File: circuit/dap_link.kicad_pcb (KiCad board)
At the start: 2 copper layers, 44.6 x 23.5 mm, 35 parts, among them J1 USB_A_CONN, J2 SWD_CONN_5P, J3 UART1_CONN_3P, J4 PAEX_CONN_8P, U1 STM32F103CBTx, U2 AMS1117-3.3, Y1 8MHz

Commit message: 新版kicad
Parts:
- removed J4: PAEX_CONN_8P, Connector_PinHeader_2.54mm:PinHeader_1x08_P2.54mm_Horizontal
- removed R11, R13, R14, R15, R16, R17, R18: 1K, Resistor_SMD:R_0603_1608Metric_Pad1.05x0.95mm_HandSolder
- added J5: Conn_02x10_Odd_Even, Connector_PinSocket_2.54mm:PinSocket_2x10_P2.54mm_Horizontal, B.Cu at (150.5, 114.7)
- added U3: TXS0108EPW, Package_SO:TSSOP-20_4.4x6.5mm_P0.65mm, F.Cu at (141.3, 104.1)
- C1, C2, C3, C4, C7, C8: footprint Capacitor_SMD:C_0603_1608Metric_Pad1.05x0.95mm_HandSolder -> Capacitor_SMD:C_0805_2012Metric_Pad1.18x1.45mm_HandSolder
- R1, R10, R12, R2, R3, R4, R5, R6, R7, R8, R9: footprint Resistor_SMD:R_0603_1608Metric_Pad1.05x0.95mm_HandSolder -> Resistor_SMD:R_0805_2012Metric_Pad1.20x1.40mm_HandSolder
- Y1: footprint Crystal:Crystal_SMD_HC49-SD -> Crystal:Crystal_SMD_5032-2Pin_5.0x3.2mm_HandSoldering
- moved C7 2.16 mm to (126.3, 125.9)
- moved Y1 1.97 mm to (123.0, 127.8)
- moved C4 1.92 mm to (126.2, 130.4)
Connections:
- U1 pad 17: /LEDR_GPIO -> /PA7
- U1 pad 18: Net-(U1-Pad18) -> /PB0
- U1 pad 19: Net-(U1-Pad19) -> /LEDR_GPIO
- U1 pad 2: Net-(U1-Pad2) -> unconnected-(U1-PC13-Pad2)
- U1 pad 20: Net-(U1-Pad20) -> /LEDG_GPIO
- U1 pad 21: Net-(U1-Pad21) -> unconnected-(U1-PB10-Pad21)
- U1 pad 22: Net-(U1-Pad22) -> unconnected-(U1-PB11-Pad22)
- U1 pad 25: Net-(U1-Pad25) -> unconnected-(U1-PB12-Pad25)
- U1 pad 26: Net-(U1-Pad26) -> unconnected-(U1-PB13-Pad26)
- U1 pad 27: Net-(U1-Pad27) -> unconnected-(U1-PB14-Pad27)
- U1 pad 28: Net-(U1-Pad28) -> unconnected-(U1-PB15-Pad28)
- U1 pad 29: /LEDG_GPIO -> unconnected-(U1-PA8-Pad29)
- U1 pad 3: Net-(U1-Pad3) -> unconnected-(U1-PC14-Pad3)
- U1 pad 38: Net-(U1-Pad38) -> unconnected-(U1-PA15-Pad38)
- U1 pad 39: Net-(U1-Pad39) -> unconnected-(U1-PB3-Pad39)
- U1 pad 4: Net-(U1-Pad4) -> unconnected-(U1-PC15-Pad4)
- U1 pad 40: Net-(U1-Pad40) -> unconnected-(U1-PB4-Pad40)
- U1 pad 41: Net-(U1-Pad41) -> unconnected-(U1-PB5-Pad41)
- U1 pad 42: Net-(U1-Pad42) -> unconnected-(U1-PB6-Pad42)
- U1 pad 43: Net-(U1-Pad43) -> unconnected-(U1-PB7-Pad43)
- U1 pad 45: Net-(U1-Pad45) -> unconnected-(U1-PB8-Pad45)
- U1 pad 46: Net-(U1-Pad46) -> unconnected-(U1-PB9-Pad46)
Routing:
- net /PA6: track 15.7 -> 0.00 mm
- net /PA5: track 14.5 -> 0.00 mm
- net Net-(C7-Pad1): track 13.5 -> 0.00 mm
- net /PA4: track 13.2 -> 0.00 mm
- net +3V3: track 75.7 -> 64.0 mm, vias 3 -> 2
- net /PA3: track 11.6 -> 0.00 mm
- net /PA0: track 11.1 -> 0.00 mm
- net /PA1: track 10.6 -> 0.00 mm
- net /LEDG_GPIO: track 10.9 -> 0.48 mm
- net Net-(J4-Pad8): track 10.3 -> 0.00 mm
- net /PA2: track 10.1 -> 0.00 mm
- net /OSC_IN: track 13.0 -> 3.05 mm
- net Net-(J4-Pad7): track 9.52 -> 0.00 mm
- net Net-(J4-Pad6): track 9.12 -> 0.00 mm
- net Net-(J4-Pad5): track 8.05 -> 0.00 mm
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- removed copper zone on B.Cu, net GND
- removed copper zone on F.Cu, net GND
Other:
- board outline removed
- net class Default removed

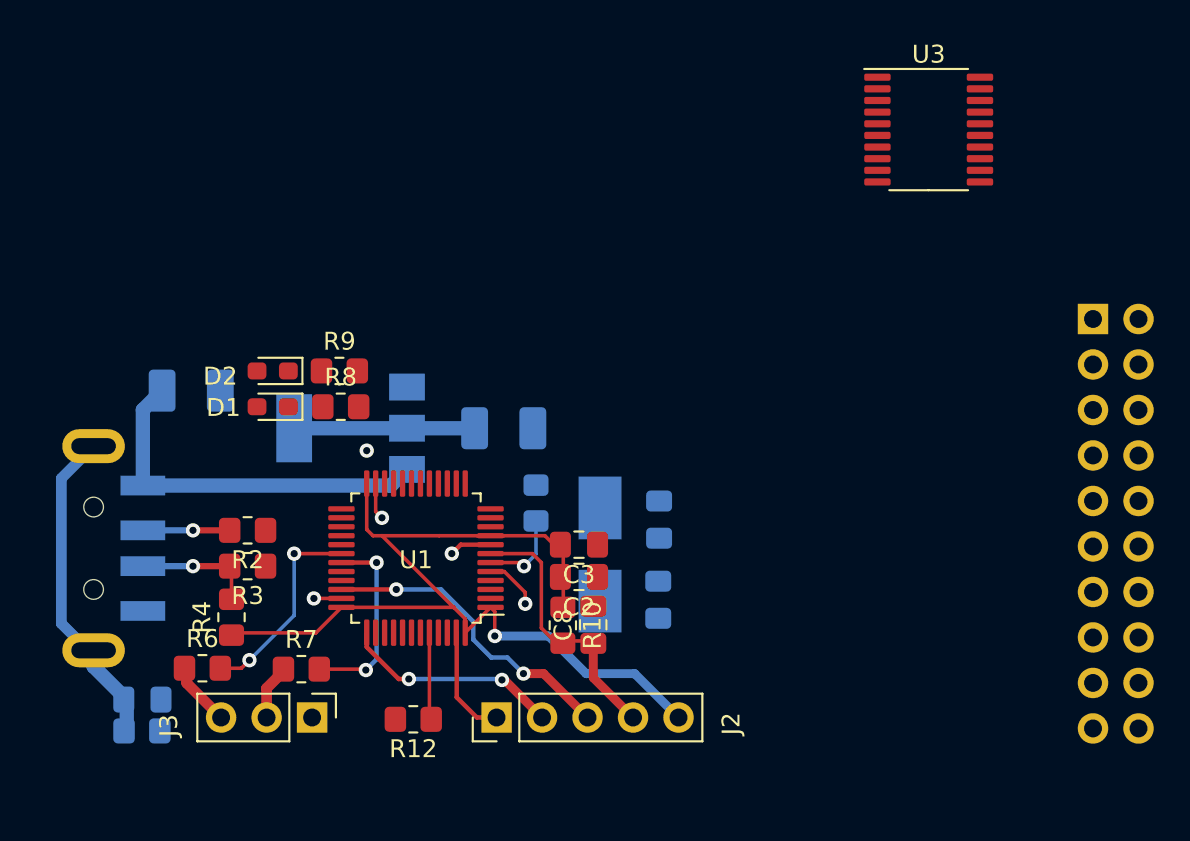
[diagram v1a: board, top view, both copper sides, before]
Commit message: kicad有DRC错误
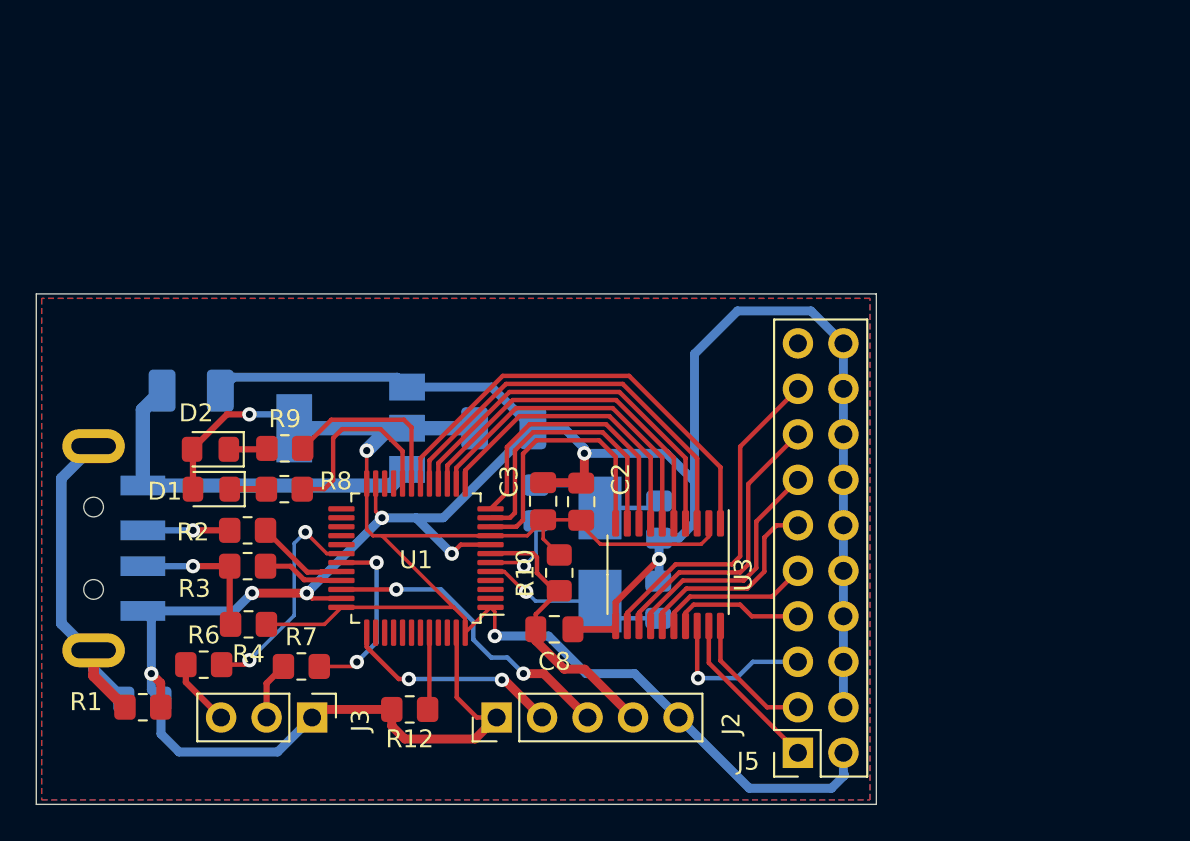
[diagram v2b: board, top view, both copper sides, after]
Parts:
- D1, D2: footprint LED_SMD:LED_0603_1608Metric_Pad1.05x0.95mm_HandSolder -> Diode_SMD:D_0805_2012Metric_Pad1.15x1.40mm_HandSolder
- J5: footprint Connector_PinSocket_2.54mm:PinSocket_2x10_P2.54mm_Horizontal -> Connector_PinSocket_2.54mm:PinSocket_2x10_P2.54mm_Vertical; moved to F.Cu
- R1: moved to F.Cu
- moved J5 29.3 mm to (134.0, 138.9)
- moved U3 28.8 mm to (126.8, 129.0), turned to -90 degrees
- moved D1 5.74 mm to (101.3, 124.2)
- moved D2 5.59 mm to (101.2, 122.0)
- moved R8 5.58 mm to (105.3, 124.2)
- moved R9 5.29 mm to (105.4, 121.9)
- moved C2 4.20 mm to (121.9, 124.9), turned to -90 degrees
- moved C3 3.14 mm to (119.8, 124.9), turned to -90 degrees
- moved R10 2.93 mm to (120.7, 128.9)
- moved C8 2.19 mm to (120.4, 132.0), turned to 0 degrees
- moved R1 1.33 mm to (97.5, 136.4)
- moved R4 1.03 mm to (103.3, 131.8), turned to 180 degrees
- moved R12 0.59 mm to (112.3, 136.5)
- moved R6 0.21 mm to (100.8, 134.0)
- moved R7 0.15 mm to (106.3, 134.1)
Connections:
- C8 pad 1: /NRST -> /MCU_RST
- J2 pad 4: /NRST -> /MCU_RST
- R10 pad 2: /NRST -> /MCU_RST
- U1 pad 7: /NRST -> /MCU_RST
- U3 pad 1: /PA1 -> /PB0
- U3 pad 3: /PA2 -> /PA7
- U3 pad 4: /PA3 -> /PA6
- U3 pad 5: /PA4 -> /PA5
- U3 pad 6: /PA5 -> /PA4
- U3 pad 7: /PA6 -> /PA3
- U3 pad 8: /PA7 -> /PA2
- U3 pad 9: /PB0 -> /PA1
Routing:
- net GND: track 12.9 -> 157.9 mm, vias 3 -> 7
- net +3V3: track 64.0 -> 96.6 mm, vias 2 -> 3
- net /PB0: track 0.00 -> 25.3 mm
- net /PA7: track 0.00 -> 23.4 mm
- net /PA6: track 0.00 -> 21.8 mm
- net /PA5: track 0.00 -> 20.2 mm
- net /RES_IO: track 0.00 -> 19.0 mm
- net /PA4: track 0.00 -> 18.6 mm
- net /PA3: track 0.00 -> 17.0 mm
- net /PA2: track 0.00 -> 16.2 mm
- net /PA1: track 0.00 -> 15.9 mm
- net /MCU_RST: track 0.00 -> 15.8 mm
- net /PA0: track 0.00 -> 15.2 mm
- net /TDO: track 0.00 -> 13.6 mm
- net /RTCK_UNUSED: track 0.00 -> 11.4 mm
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- added copper zone on B.Cu, net GND
- added copper zone on F.Cu, net GND
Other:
- board outline added: 46.9 x 28.5 mm

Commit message: DRC通过
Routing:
- net GND: vias 7 -> 32
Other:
- board size 46.9 x 28.5 mm -> 47.1 x 28.5 mm
- rule pad_to_mask_clearance: 0.051 -> 0
